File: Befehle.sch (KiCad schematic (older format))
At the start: 55 parts, among them P1 CONN_02X10, P2 CONN_02X10, P3 CONN_01X01, P4 CONN_01X01, U1 74LS14, U2 74540, U3 7400, U4 74HCT02, U5 74LS541, U6 74LS373, U7 74LS139, U8 74LS540

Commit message: Befehle: Headers, Schraubkontakte Terminal Blocks, Kondensatoren eingefügt
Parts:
- removed P3, P4: CONN_01X01, Pin_Headers:Pin_Header_Straight_1x01_Pitch1.27mm, symbol conn:CONN_01X01
- added C1, C2: 100n, symbol bonsai:C_Small
- added J1, J? (x3): 2PinTerminalBlocktg, 2PinTerminalBlocktg, symbol 2PinTerminalBlocktg:2PinTerminalBlocktg
- added J?: 3PinTerminalBlocktg, 3PinTerminalBlocktg, symbol 3PinTerminalBlocktg:3PinTerminalBlocktg
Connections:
- wire segments 278 -> 285
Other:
- moved on the sheet: D22

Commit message: tracks gelegt
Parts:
- U2: footprint Housings_DIP:DIP-20_W7.62mm_LongPads -> Housings_DIP:DIP-20_W7.62mm_Socket_LongPads
- gave numbers to parts that had none: 4
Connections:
- wire segments 285 -> 263
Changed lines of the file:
@@
 F 0 "U2" H -8850 4600 60  0000 C CNN
 F 1 "74540" H -8800 4350 60  0000 C CNN
-F 2 "Housings_DIP:DIP-20_W7.62mm_LongPads" H -8800 4350 60  0001 C CNN
+F 2 "Housings_DIP:DIP-20_W7.62mm_Socket_LongPads" H -8800 4350 60  0001 C CNN
 F 3 "" H -8800 4350 60  0001 C CNN
 	8    -8950 4500
@@
 F 0 "U2" H -4750 8450 60  0000 C CNN
 F 1 "74540" H -4700 8200 60  0000 C CNN
-F 2 "Housings_DIP:DIP-20_W7.62mm_LongPads" H -4700 8200 60  0001 C CNN
+F 2 "Housings_DIP:DIP-20_W7.62mm_Socket_LongPads" H -4700 8200 60  0001 C CNN
 F 3 "" H -4700 8200 60  0001 C CNN
 	4    -4850 8350
@@
 F 0 "U2" H -4300 8450 60  0000 C CNN
 F 1 "74540" H -4250 8200 60  0000 C CNN
-F 2 "Housings_DIP:DIP-20_W7.62mm_LongPads" H -4250 8200 60  0001 C CNN
+F 2 "Housings_DIP:DIP-20_W7.62mm_Socket_LongPads" H -4250 8200 60  0001 C CNN
 F 3 "" H -4250 8200 60  0001 C CNN
 	3    -4400 8350
@@
 F 0 "U2" H -3800 8450 60  0000 C CNN
 F 1 "74540" H -3750 8200 60  0000 C CNN
-F 2 "Housings_DIP:DIP-20_W7.62mm_LongPads" H -3750 8200 60  0001 C CNN
+F 2 "Housings_DIP:DIP-20_W7.62mm_Socket_LongPads" H -3750 8200 60  0001 C CNN
 F 3 "" H -3750 8200 60  0001 C CNN
 	2    -3900 8350
@@
 F 0 "U2" H -7650 3100 60  0000 C CNN
 F 1 "74540" H -7600 2850 60  0000 C CNN
-F 2 "Housings_DIP:DIP-20_W7.62mm_LongPads" H -7600 2850 60  0001 C CNN
+F 2 "Housings_DIP:DIP-20_W7.62mm_Socket_LongPads" H -7600 2850 60  0001 C CNN
 F 3 "" H -7600 2850 60  0001 C CNN
 	7    -7750 3000
@@
 Connection ~ -8300 5050
 Wire Wire Line
-	-8300 5050 -8300 5600
-Connection ~ -8300 5600
-Wire Wire Line
-	-8300 5600 -8300 6150
-Connection ~ -8300 6150
-Wire Wire Line
 	-8300 4900 -8300 5050
 Wire Wire Line
 	-8300 4500 -8300 5050
-Wire Wire Line
-	-8300 6150 -8300 6650
 Wire Bus Line
 	37900 55900 37900 44500
@@
 Wire Wire Line
 	-2900 8500 -2900 8750
-Wire Wire Line
-	-6550 -1050 -6450 -1050
-Connection ~ -5550 -1050
-Wire Wire Line
-	-5550 -1050 -5450 -1050
-Connection ~ -6450 -1050
-Wire Wire Line
-	-6450 -1050 -6350 -1050
-Connection ~ -6350 -1050
-Wire Wire Line
-	-6350 -1050 -6250 -1050
-Connection ~ -6250 -1050
-Wire Wire Line
-	-6250 -1050 -6150 -1050
-Connection ~ -6150 -1050
-Wire Wire Line
-	-6150 -1050 -6050 -1050
-Connection ~ -6050 -1050
-Wire Wire Line
-	-6050 -1050 -5950 -1050
-Connection ~ -5950 -1050
-Wire Wire Line
-	-5950 -1050 -5850 -1050
-Connection ~ -5850 -1050
-Wire Wire Line
-	-5850 -1050 -5750 -1050
-Connection ~ -5750 -1050
-Wire Wire Line
-	-5750 -1050 -5650 -1050
-Connection ~ -5650 -1050
-Wire Wire Line
-	-5650 -1050 -5550 -1050
-Wire Wire Line
-	-6850 7400 -6700 7400
-Connection ~ -6700 7400
-Wire Wire Line
-	-6700 7400 -6600 7400
-Connection ~ -5800 7400
-Wire Wire Line
-	-5800 7400 -5650 7400
-Connection ~ -6600 7400
-Wire Wire Line
-	-6600 7400 -6500 7400
-Connection ~ -6500 7400
-Wire Wire Line
-	-6500 7400 -6400 7400
-Connection ~ -6400 7400
-Wire Wire Line
-	-6400 7400 -6300 7400
-Connection ~ -6300 7400
-Wire Wire Line
-	-6300 7400 -6200 7400
-Connection ~ -6200 7400
-Wire Wire Line
-	-6200 7400 -6100 7400
-Connection ~ -6100 7400
-Wire Wire Line
-	-6100 7400 -6000 7400
-Connection ~ -6000 7400
-Wire Wire Line
-	-6000 7400 -5900 7400
-Connection ~ -5900 7400
-Wire Wire Line
-	-5900 7400 -5800 7400
 $Comp
 L 2PinTerminalBlocktg:2PinTerminalBlocktg J1
@@
 	1750 7300 1950 7300
 $Comp
-L 2PinTerminalBlocktg:2PinTerminalBlocktg J?
+L 2PinTerminalBlocktg:2PinTerminalBlocktg J4
 U 1 1 5ADB99D1
 P -1850 6950
-F 0 "J?" H -1885 6940 50  0000 L CNN
+F 0 "J4" H -1885 6940 50  0000 L CNN
 F 1 "2PinTerminalBlocktg" H -1885 6849 50  0000 L CNN
 F 2 "2PinTerminalBlocktg" H -1850 6950 50  0001 L BNN
@@
 $EndComp
 $Comp
-L 2PinTerminalBlocktg:2PinTerminalBlocktg J?
+L 2PinTerminalBlocktg:2PinTerminalBlocktg J5
 U 1 1 5ADB9B3E
 P -1850 7150
-F 0 "J?" H -1885 7140 50  0000 L CNN
+F 0 "J5" H -1885 7140 50  0000 L CNN
 F 1 "2PinTerminalBlocktg" H -1885 7049 50  0000 L CNN
 F 2 "2PinTerminalBlocktg" H -1850 7150 50  0001 L BNN
@@
 $EndComp
 $Comp
-L 2PinTerminalBlocktg:2PinTerminalBlocktg J?
+L 2PinTerminalBlocktg:2PinTerminalBlocktg J2
 U 1 1 5ADBA454
 P -11150 1900
-F 0 "J?" H -11288 1586 50  0000 C CNN
+F 0 "J2" H -11288 1586 50  0000 C CNN
 F 1 "2PinTerminalBlocktg" H -11288 1677 50  0000 C CNN
 F 2 "2PinTerminalBlocktg" H -11150 1900 50  0001 L BNN
@@
 $EndComp
 $Comp
-L 3PinTerminalBlocktg:3PinTerminalBlocktg J?
+L 3PinTerminalBlocktg:3PinTerminalBlocktg J3
 U 1 1 5ADBA737
 P -10750 7250
-F 0 "J?" H -10888 6936 50  0000 C CNN
+F 0 "J3" H -10888 6936 50  0000 C CNN
 F 1 "3PinTerminalBlocktg" H -10888 7027 50  0000 C CNN
 F 2 "3PinTerminalBlocktg" H -10750 7250 50  0001 L BNN
@@
 Wire Wire Line
 	-2200 7250 -2050 7250
+Wire Wire Line
+	-8300 5050 -8300 6650
+Wire Wire Line
+	-6550 -1050 -5450 -1050
+Wire Wire Line
+	-6850 7400 -5650 7400
 Wire Bus Line
 	-6500 6800 -6300 6800

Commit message: wires gelegt
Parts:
- U1: symbol 74xx:74LS14 -> Befehle-rescue:74LS14-RESCUE-Befehle
- U3: symbol 74xx:7400 -> Befehle-rescue:7400-RESCUE-Befehle
- U4: symbol 74xx:74HCT02 -> Befehle-rescue:74HCT02-RESCUE-Befehle
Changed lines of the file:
@@
 $EndComp
 $Comp
-L 74xx:74HCT02 U4
+L Befehle-rescue:74HCT02-RESCUE-Befehle U4
 U 1 1 57F2C440
 P -7700 4500
@@
 $EndComp
 $Comp
-L 74xx:74HCT02 U4
+L Befehle-rescue:74HCT02-RESCUE-Befehle U4
 U 2 1 57F2C605
 P -7700 5050
@@
 $EndComp
 $Comp
-L 74xx:74HCT02 U4
+L Befehle-rescue:74HCT02-RESCUE-Befehle U4
 U 3 1 57F2C694
 P -7700 5600
@@
 $EndComp
 $Comp
-L 74xx:74HCT02 U4
+L Befehle-rescue:74HCT02-RESCUE-Befehle U4
 U 4 1 57F2C76F
 P -7700 6150
@@
 $EndComp
 $Comp
-L 74xx:7400 U3
+L Befehle-rescue:7400-RESCUE-Befehle U3
 U 2 1 57F3278C
 P -8400 7250
@@
 $EndComp
 $Comp
-L 74xx:7400 U3
+L Befehle-rescue:7400-RESCUE-Befehle U3
 U 3 1 57F32988
 P -8300 8450
@@
 $EndComp
 $Comp
-L 74xx:7400 U3
+L Befehle-rescue:7400-RESCUE-Befehle U3
 U 4 1 57F32A39
 P -7650 8850
@@
 $EndComp
 $Comp
-L 74xx:7400 U3
+L Befehle-rescue:7400-RESCUE-Befehle U3
 U 1 1 57F331B6
 P -8650 6050
@@
 	-8200 3000 -8100 3000
 $Comp
-L 74xx:74LS14 U1
+L Befehle-rescue:74LS14-RESCUE-Befehle U1
 U 2 1 5A2A45AB
 P -8800 1400
@@
 $EndComp
 $Comp
-L 74xx:74LS14 U1
+L Befehle-rescue:74LS14-RESCUE-Befehle U1
 U 1 1 5A2A5408
 P -9250 950
@@
 $EndComp
 $Comp
-L 74xx:74LS14 U1
+L Befehle-rescue:74LS14-RESCUE-Befehle U1
 U 3 1 5A2A55C6
 P -8300 950
@@
 Text GLabel -10350 7350 2    60   Input ~ 0
 upPC
+Text GLabel -10350 7150 2    60   Input ~ 0
+incPC
 Text GLabel -10350 7250 2    60   Input ~ 0
-incPC
-Text GLabel -10350 7150 2    60   Input ~ 0
 incPCz
-Wire Wire Line
-	-10350 7150 -10550 7150
-Wire Wire Line
-	-10550 7250 -10350 7250
 Wire Wire Line
 	-10350 7350 -10550 7350
@@
 Wire Wire Line
 	-6850 7400 -5650 7400
+Wire Wire Line
+	-10550 7150 -10350 7150
+Wire Wire Line
+	-10550 7250 -10350 7250
 Wire Bus Line
 	-6500 6800 -6300 6800

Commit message: wires gelegt
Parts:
- added unit 6 of U1
- added unit 5 of U1
- added unit 4 of U1
- C1, C2: footprint (none) -> Capacitors_ThroughHole:C_Disc_D10.0mm_W2.5mm_P5.00mm
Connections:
- wire segments 263 -> 220
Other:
- moved on the sheet: U1B, U1C

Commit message: tracks gelegt und so
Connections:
- wire segments 220 -> 285

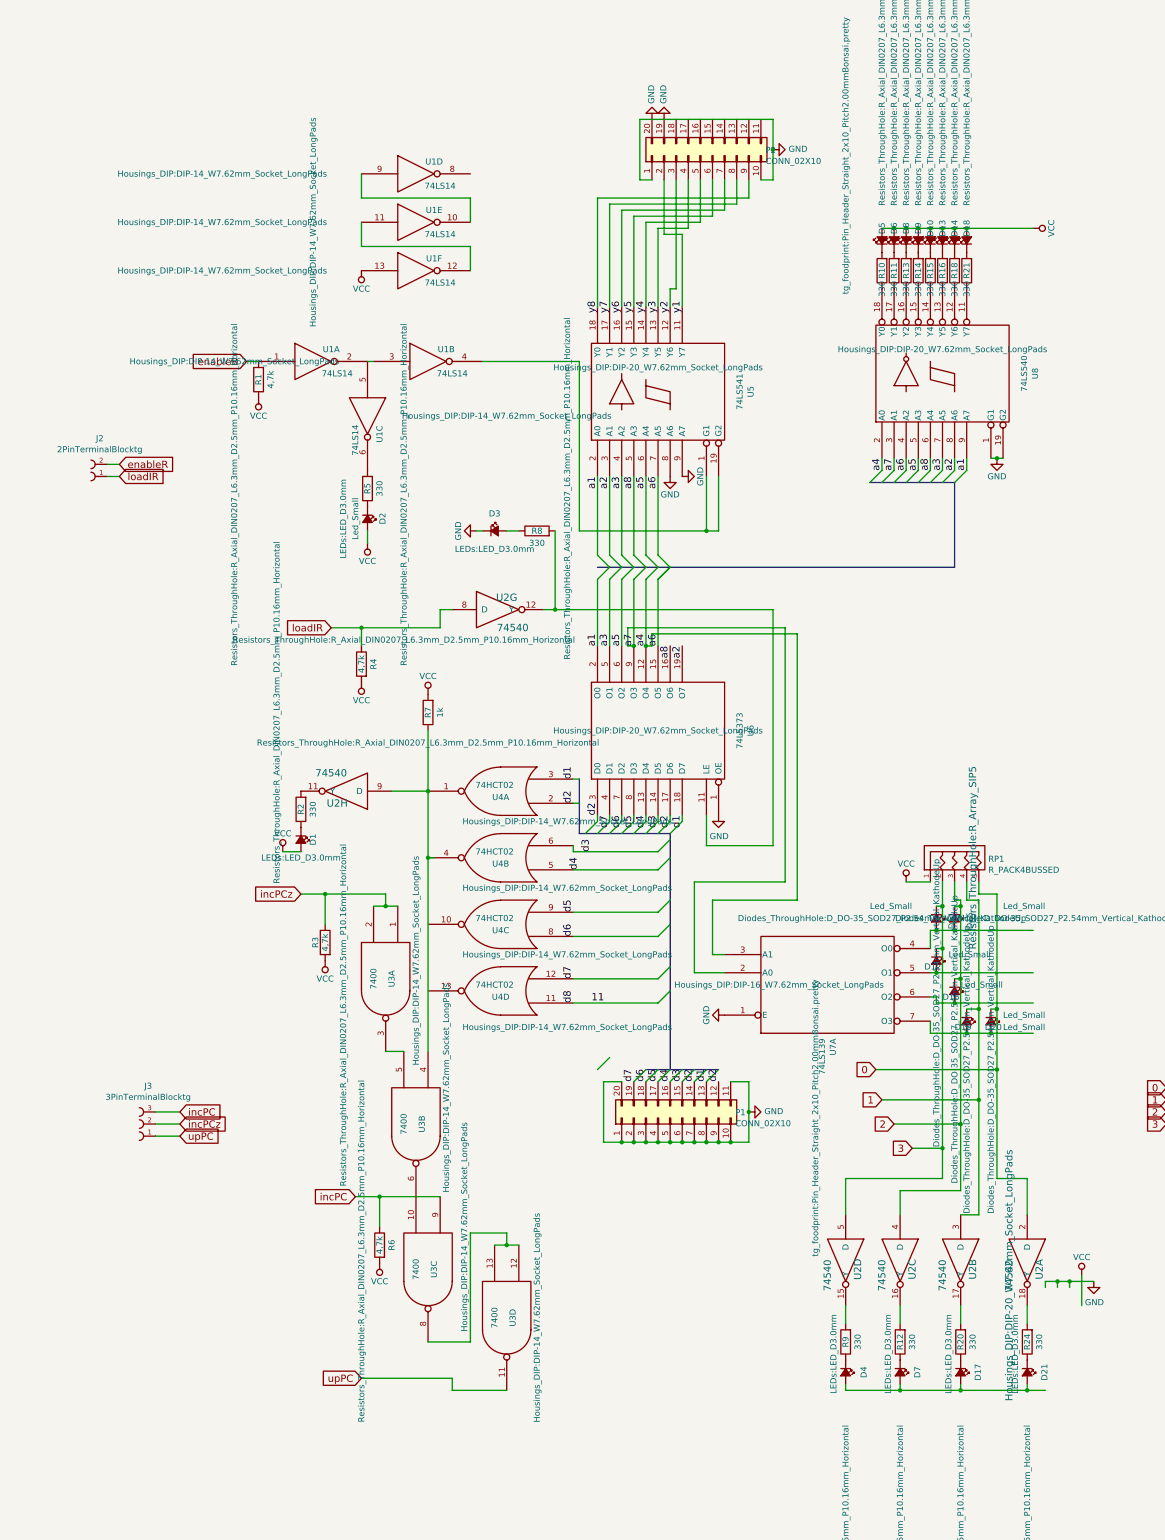
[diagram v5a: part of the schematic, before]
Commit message: todos done (netze entflechten), some footprintslocaliszed
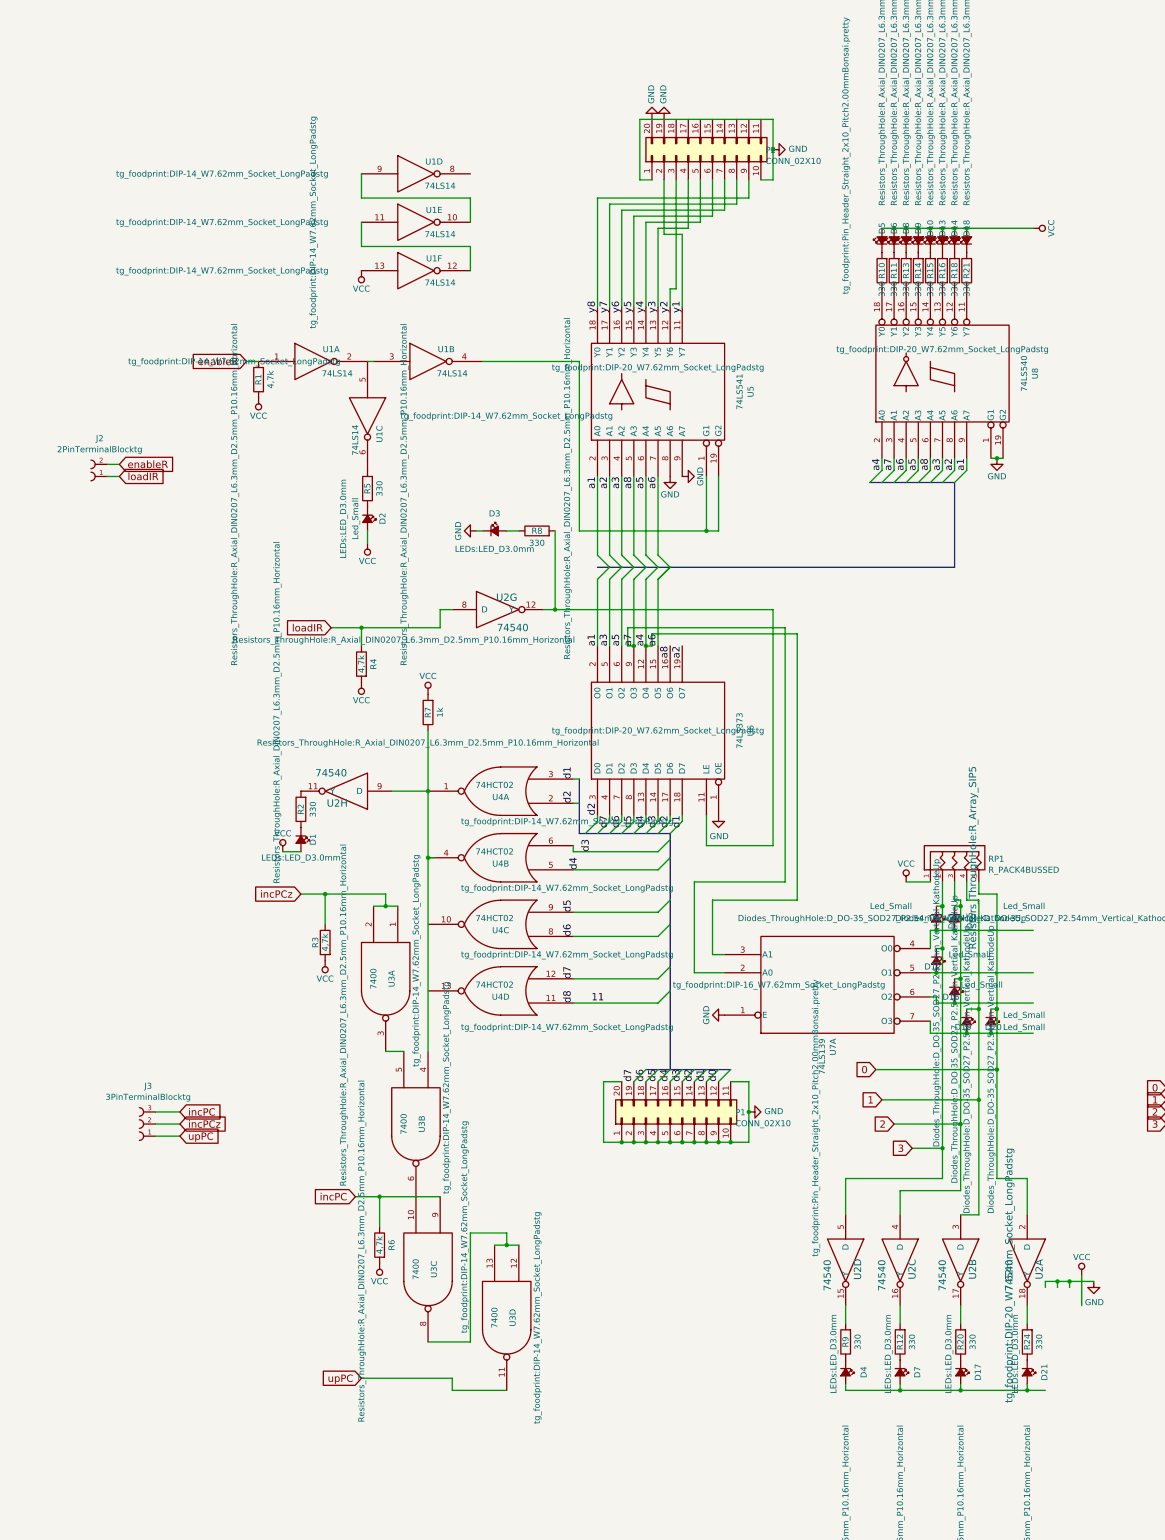
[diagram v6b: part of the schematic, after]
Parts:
- U1, U3, U4: footprint Housings_DIP:DIP-14_W7.62mm_Socket_LongPads -> tg_foodprint:DIP-14_W7.62mm_Socket_LongPadstg
- U2, U5, U6, U8: footprint Housings_DIP:DIP-20_W7.62mm_Socket_LongPads -> tg_foodprint:DIP-20_W7.62mm_Socket_LongPadstg
- U7: footprint Housings_DIP:DIP-16_W7.62mm_Socket_LongPads -> tg_foodprint:DIP-16_W7.62mm_Socket_LongPadstg
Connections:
- net labels added: d0
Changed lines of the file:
@@
 F 0 "U6" H -6400 3234 50  0000 C CNN
 F 1 "74LS373" H -6400 3325 50  0000 C CNN
-F 2 "Housings_DIP:DIP-20_W7.62mm_Socket_LongPads" V -6400 4000 50  0000 C CNN
+F 2 "tg_foodprint:DIP-20_W7.62mm_Socket_LongPadstg" V -6400 4000 50  0000 C CNN
 F 3 "" H -6400 4000 50  0000 C CNN
 	1    -6400 4000
@@
 F 0 "U5" H -6400 434 50  0000 C CNN
 F 1 "74LS541" H -6400 525 50  0000 C CNN
-F 2 "Housings_DIP:DIP-20_W7.62mm_Socket_LongPads" V -6200 1200 50  0000 C CNN
+F 2 "tg_foodprint:DIP-20_W7.62mm_Socket_LongPadstg" V -6200 1200 50  0000 C CNN
 F 3 "" H -6400 1200 50  0000 C CNN
 	1    -6400 1200
@@
 F 0 "U7" V -4954 5657 50  0000 R CNN
 F 1 "74LS139" V -5045 5657 50  0000 R CNN
-F 2 "Housings_DIP:DIP-16_W7.62mm_Socket_LongPads" H -5400 6100 50  0000 C CNN
+F 2 "tg_foodprint:DIP-16_W7.62mm_Socket_LongPadstg" H -5400 6100 50  0000 C CNN
 F 3 "" H -5000 6100 50  0000 C CNN
 	1    -5000 6100
@@
 F 0 "U4" H -7700 4550 50  0000 C CNN
 F 1 "74HCT02" H -7650 4450 50  0000 C CNN
-F 2 "Housings_DIP:DIP-14_W7.62mm_Socket_LongPads" H -8250 4750 50  0000 C CNN
+F 2 "tg_foodprint:DIP-14_W7.62mm_Socket_LongPadstg" H -8250 4750 50  0000 C CNN
 F 3 "" H -7700 4500 50  0000 C CNN
 	1    -7700 4500
@@
 F 0 "U4" H -7700 5100 50  0000 C CNN
 F 1 "74HCT02" H -7650 5000 50  0000 C CNN
-F 2 "Housings_DIP:DIP-14_W7.62mm_Socket_LongPads" H -8250 5300 50  0000 C CNN
+F 2 "tg_foodprint:DIP-14_W7.62mm_Socket_LongPadstg" H -8250 5300 50  0000 C CNN
 F 3 "" H -7700 5050 50  0000 C CNN
 	2    -7700 5050
@@
 F 0 "U4" H -7700 5650 50  0000 C CNN
 F 1 "74HCT02" H -7650 5550 50  0000 C CNN
-F 2 "Housings_DIP:DIP-14_W7.62mm_Socket_LongPads" H -8250 5850 50  0000 C CNN
+F 2 "tg_foodprint:DIP-14_W7.62mm_Socket_LongPadstg" H -8250 5850 50  0000 C CNN
 F 3 "" H -7700 5600 50  0000 C CNN
 	3    -7700 5600
@@
 F 0 "U4" H -7700 6200 50  0000 C CNN
 F 1 "74HCT02" H -7650 6100 50  0000 C CNN
-F 2 "Housings_DIP:DIP-14_W7.62mm_Socket_LongPads" H -8250 6450 50  0000 C CNN
+F 2 "tg_foodprint:DIP-14_W7.62mm_Socket_LongPadstg" H -8250 6450 50  0000 C CNN
 F 3 "" H -7700 6150 50  0000 C CNN
 	4    -7700 6150
@@
 F 0 "U8" H -4050 284 50  0000 C CNN
 F 1 "74LS540" H -4050 375 50  0000 C CNN
-F 2 "Housings_DIP:DIP-20_W7.62mm_Socket_LongPads" V -3850 1050 50  0000 C CNN
+F 2 "tg_foodprint:DIP-20_W7.62mm_Socket_LongPadstg" V -3850 1050 50  0000 C CNN
 F 3 "" H -4050 1050 50  0000 C CNN
 	1    -4050 1050
@@
 F 0 "U3" H -8400 7300 50  0000 C CNN
 F 1 "7400" H -8400 7150 50  0000 C CNN
-F 2 "Housings_DIP:DIP-14_W7.62mm_Socket_LongPads" H -8700 7500 50  0000 C CNN
+F 2 "tg_foodprint:DIP-14_W7.62mm_Socket_LongPadstg" H -8700 7500 50  0000 C CNN
 F 3 "" H -8400 7250 50  0000 C CNN
 	2    -8400 7250
@@
 F 0 "U3" H -8300 8500 50  0000 C CNN
 F 1 "7400" H -8300 8350 50  0000 C CNN
-F 2 "Housings_DIP:DIP-14_W7.62mm_Socket_LongPads" H -8650 8750 50  0000 C CNN
+F 2 "tg_foodprint:DIP-14_W7.62mm_Socket_LongPadstg" H -8650 8750 50  0000 C CNN
 F 3 "" H -8300 8450 50  0000 C CNN
 	3    -8300 8450
@@
 F 0 "U3" H -7650 8900 50  0000 C CNN
 F 1 "7400" H -7650 8750 50  0000 C CNN
-F 2 "Housings_DIP:DIP-14_W7.62mm_Socket_LongPads" H -7650 9100 50  0000 C CNN
+F 2 "tg_foodprint:DIP-14_W7.62mm_Socket_LongPadstg" H -7650 9100 50  0000 C CNN
 F 3 "" H -7650 8850 50  0000 C CNN
 	4    -7650 8850
@@
 F 0 "U3" H -8650 6100 50  0000 C CNN
 F 1 "7400" H -8650 5950 50  0000 C CNN
-F 2 "Housings_DIP:DIP-14_W7.62mm_Socket_LongPads" H -8800 6300 50  0000 C CNN
+F 2 "tg_foodprint:DIP-14_W7.62mm_Socket_LongPadstg" H -8800 6300 50  0000 C CNN
 F 3 "" H -8650 6050 50  0000 C CNN
 	1    -8650 6050
@@
 F 0 "U1" H -8150 1050 50  0000 C CNN
 F 1 "74LS14" H -8100 850 50  0000 C CNN
-F 2 "Housings_DIP:DIP-14_W7.62mm_Socket_LongPads" H -9900 950 50  0000 C CNN
+F 2 "tg_foodprint:DIP-14_W7.62mm_Socket_LongPadstg" H -9900 950 50  0000 C CNN
 F 3 "" H -8300 950 50  0000 C CNN
 	2    -8300 950
@@
 F 0 "U1" H -9100 1050 50  0000 C CNN
 F 1 "74LS14" H -9050 850 50  0000 C CNN
-F 2 "Housings_DIP:DIP-14_W7.62mm_Socket_LongPads" V -9250 2100 50  0000 C CNN
+F 2 "tg_foodprint:DIP-14_W7.62mm_Socket_LongPadstg" V -9250 2100 50  0000 C CNN
 F 3 "" H -9250 950 50  0000 C CNN
 	1    -9250 950
@@
 F 0 "U1" H -8650 1500 50  0000 C CNN
 F 1 "74LS14" H -8600 1300 50  0000 C CNN
-F 2 "Housings_DIP:DIP-14_W7.62mm_Socket_LongPads" V -8800 2550 50  0000 C CNN
+F 2 "tg_foodprint:DIP-14_W7.62mm_Socket_LongPadstg" V -8800 2550 50  0000 C CNN
 F 3 "" H -8800 1400 50  0000 C CNN
 	3    -8800 1400
@@
 F 0 "U2" H -8850 4600 60  0000 C CNN
 F 1 "74540" H -8800 4350 60  0000 C CNN
-F 2 "Housings_DIP:DIP-20_W7.62mm_Socket_LongPads" H -8800 4350 60  0001 C CNN
+F 2 "tg_foodprint:DIP-20_W7.62mm_Socket_LongPadstg" H -8800 4350 60  0001 C CNN
 F 3 "" H -8800 4350 60  0001 C CNN
 	8    -8950 4500
@@
 F 0 "U2" H -4750 8450 60  0000 C CNN
 F 1 "74540" H -4700 8200 60  0000 C CNN
-F 2 "Housings_DIP:DIP-20_W7.62mm_Socket_LongPads" H -4700 8200 60  0001 C CNN
+F 2 "tg_foodprint:DIP-20_W7.62mm_Socket_LongPadstg" H -4700 8200 60  0001 C CNN
 F 3 "" H -4700 8200 60  0001 C CNN
 	4    -4850 8350
@@
 F 0 "U2" H -4300 8450 60  0000 C CNN
 F 1 "74540" H -4250 8200 60  0000 C CNN
-F 2 "Housings_DIP:DIP-20_W7.62mm_Socket_LongPads" H -4250 8200 60  0001 C CNN
+F 2 "tg_foodprint:DIP-20_W7.62mm_Socket_LongPadstg" H -4250 8200 60  0001 C CNN
 F 3 "" H -4250 8200 60  0001 C CNN
 	3    -4400 8350
@@
 F 0 "U2" H -3250 8450 60  0000 C CNN
 F 1 "74540" H -3200 8200 60  0000 C CNN
-F 2 "Housings_DIP:DIP-20_W7.62mm_Socket_LongPads" H -3200 8200 60  0000 C CNN
+F 2 "tg_foodprint:DIP-20_W7.62mm_Socket_LongPadstg" H -3200 8200 60  0000 C CNN
 F 3 "" H -3200 8200 60  0001 C CNN
 	1    -3350 8350
@@
 F 0 "U2" H -7650 3100 60  0000 C CNN
 F 1 "74540" H -7600 2850 60  0000 C CNN
-F 2 "Housings_DIP:DIP-20_W7.62mm_Socket_LongPads" H -7600 2850 60  0001 C CNN
+F 2 "tg_foodprint:DIP-20_W7.62mm_Socket_LongPadstg" H -7600 2850 60  0001 C CNN
 F 3 "" H -7600 2850 60  0001 C CNN
 	7    -7750 3000
@@
 Connection ~ -6700 7400
 Entry Wire Line
-	-6900 6800 -6800 6700
+	-5900 6900 -5800 6800
 Entry Wire Line
 	-6400 6800 -6500 6900
@@
 F 0 "U1" H -8250 300 50  0000 C CNN
 F 1 "74LS14" H -8200 100 50  0000 C CNN
-F 2 "Housings_DIP:DIP-14_W7.62mm_Socket_LongPads" H -10000 200 50  0000 C CNN
+F 2 "tg_foodprint:DIP-14_W7.62mm_Socket_LongPadstg" H -10000 200 50  0000 C CNN
 F 3 "" H -8400 200 50  0000 C CNN
 	6    -8400 200
@@
 F 0 "U1" H -8250 -100 50  0000 C CNN
 F 1 "74LS14" H -8200 -300 50  0000 C CNN
-F 2 "Housings_DIP:DIP-14_W7.62mm_Socket_LongPads" H -10000 -200 50  0000 C CNN
+F 2 "tg_foodprint:DIP-14_W7.62mm_Socket_LongPadstg" H -10000 -200 50  0000 C CNN
 F 3 "" H -8400 -200 50  0000 C CNN
 	5    -8400 -200
@@
 F 0 "U1" H -8250 -500 50  0000 C CNN
 F 1 "74LS14" H -8200 -700 50  0000 C CNN
-F 2 "Housings_DIP:DIP-14_W7.62mm_Socket_LongPads" H -10000 -600 50  0000 C CNN
+F 2 "tg_foodprint:DIP-14_W7.62mm_Socket_LongPadstg" H -10000 -600 50  0000 C CNN
 F 3 "" H -8400 -600 50  0000 C CNN
 	4    -8400 -600
@@
 	-6400 3200 -5250 3200
 Connection ~ -6500 3300
+Text Label -5900 6900 1    60   ~ 0
+d0
 Wire Bus Line
 	-6500 6800 -6300 6800
 Wire Bus Line
-	-6300 6800 -5900 6800
+	-6300 6800 -5800 6800
 Wire Bus Line
 	-4650 1950 -3950 1950
@@
 Wire Bus Line
 	-7050 4850 -6300 4850
-Text Label -5900 6900 1    60   ~ 0
-d2
 $EndSCHEMATC
